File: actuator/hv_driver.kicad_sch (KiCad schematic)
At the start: 14 parts, among them U3 DRV2665

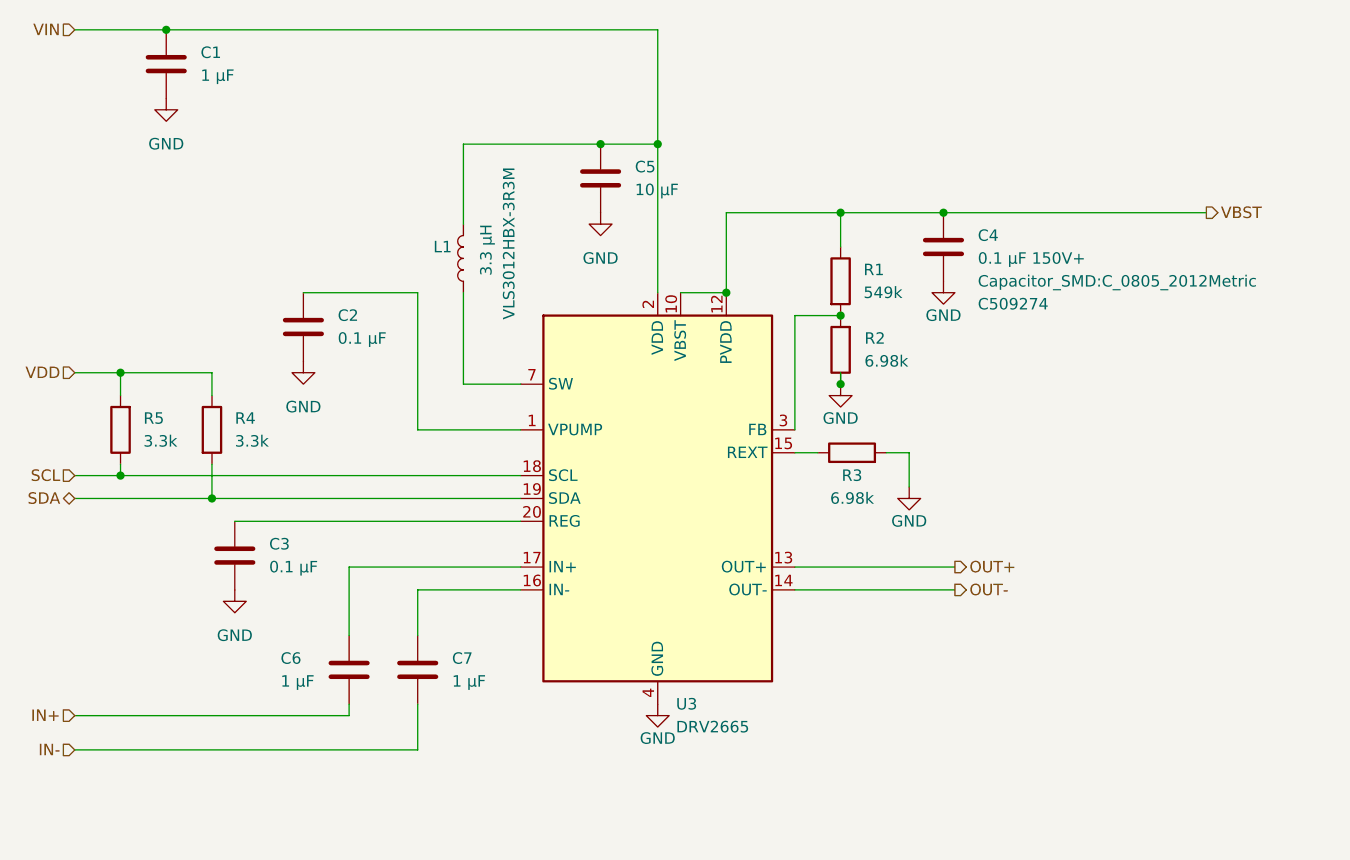
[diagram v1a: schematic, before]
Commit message: actuator move testpoints to subsheets
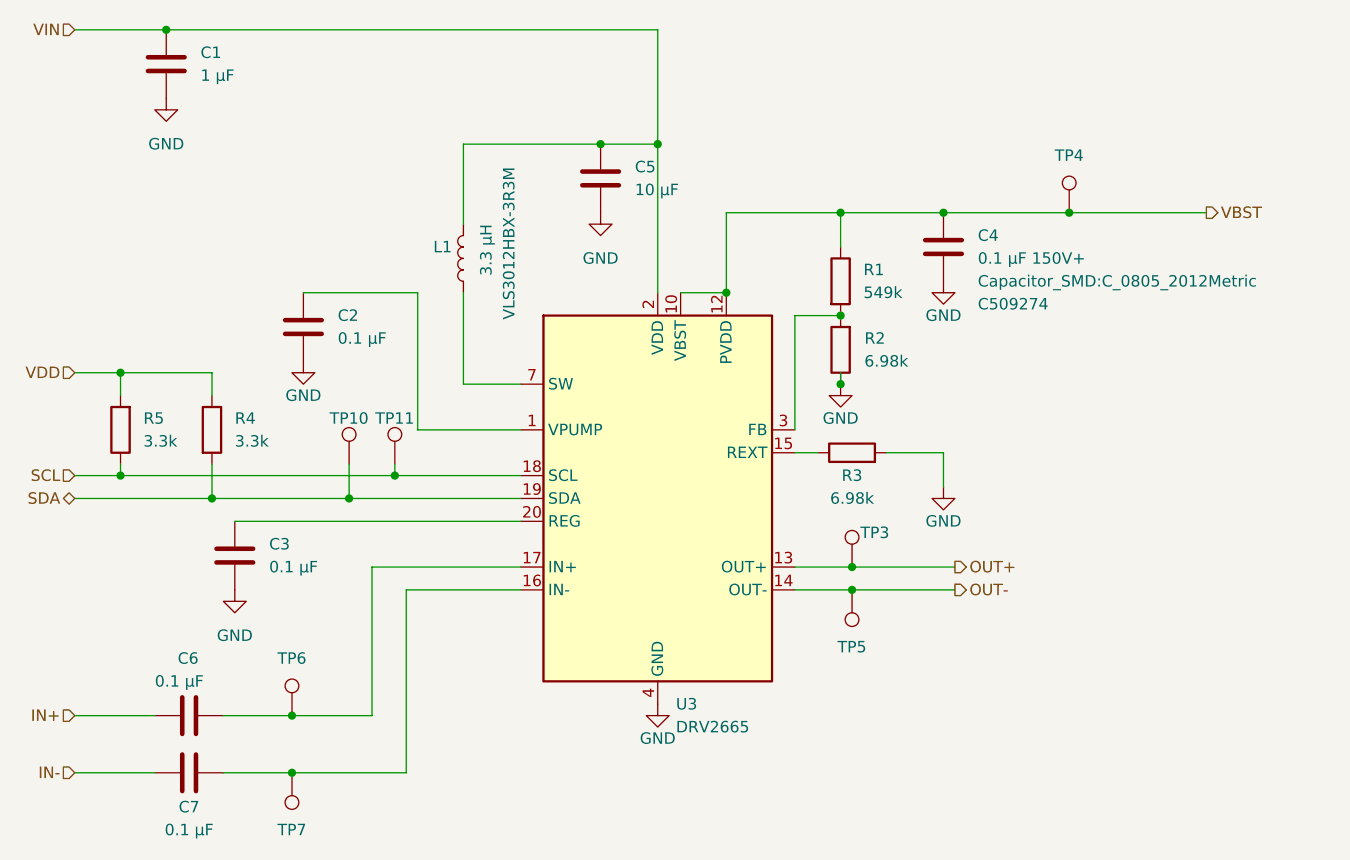
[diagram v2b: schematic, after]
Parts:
- added TP10, TP11, TP3, TP4, TP5, TP6, TP7: TestPoint, TestPoint:TestPoint_THTPad_D1.0mm_Drill0.5mm, symbol Connector:TestPoint
- C6, C7: value 1 µF -> 0.1 µF
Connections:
- net IN-: now also C7.1; no longer C7.2
- net OUT+: now also TP3.1
- net OUT-: now also TP5.1
- net SCL: now also TP11.1
- net SDA: now also TP10.1
- net VBST: now also TP4.1
- net at C6.1, U3.17 (IN+): now also TP6.1
- net at U3.16 (IN-): now also C7.2, TP7.1; no longer C7.1
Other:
- moved on the sheet: C6, C7
